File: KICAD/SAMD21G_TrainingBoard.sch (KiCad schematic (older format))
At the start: 65 parts, among them CN1 CN-PICkit4_ARM, CN2 USB_Mini_B, CN3 UART-FTDI-TTL-232R-3V3, CN4 USB_A, CN5 CN-POWER, IC1 SAMD21G18A, IC2 NJM2391DL1-33, IC3 GT20L16J1Y, SW1 SW_PUSH_2, SW2 SW_PUSH_2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

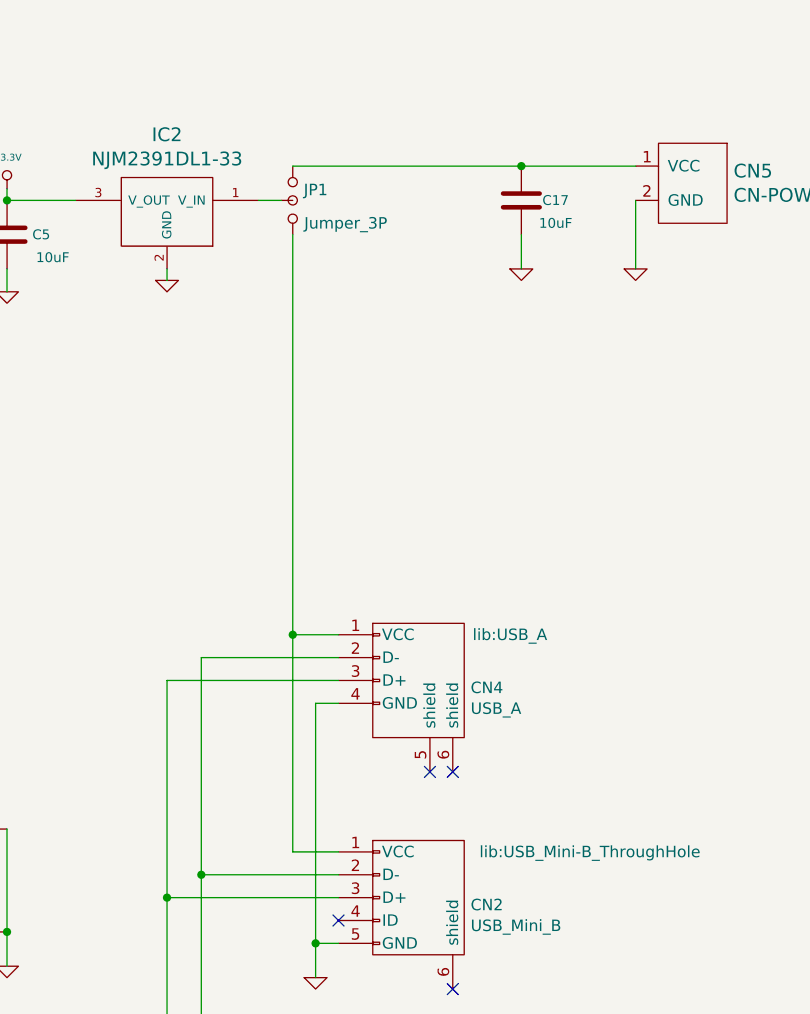
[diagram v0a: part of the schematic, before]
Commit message: amend USB Type A connector Power Supply
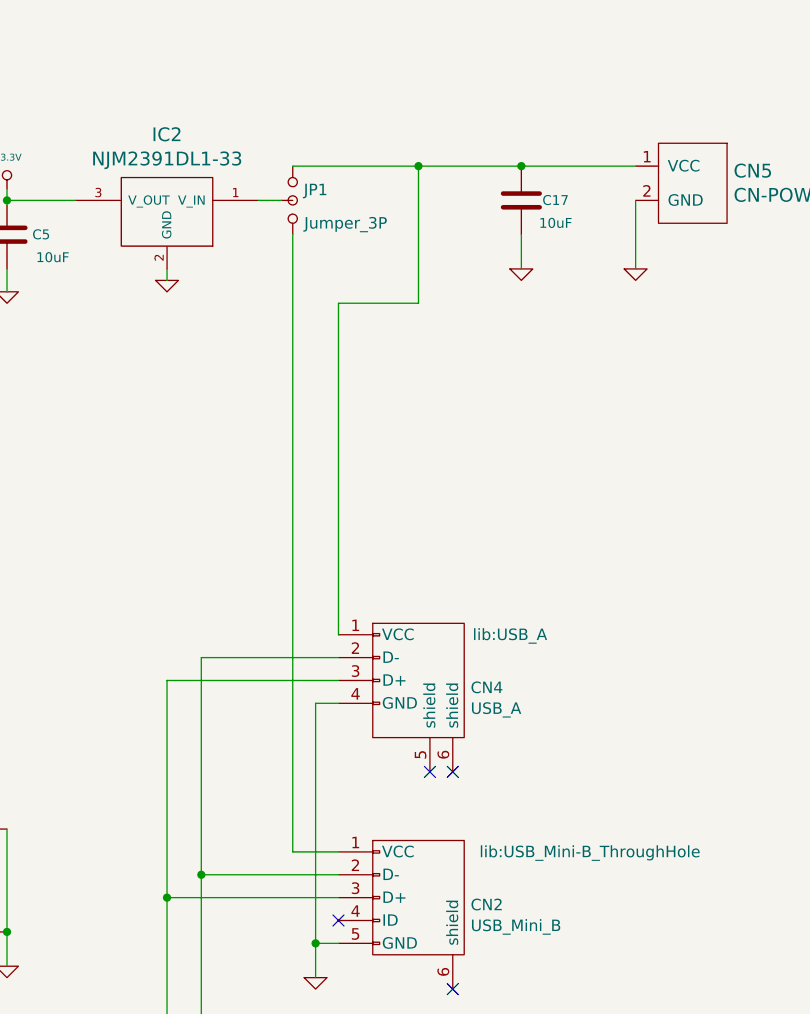
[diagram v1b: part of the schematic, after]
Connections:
- net at CN2.1 (VCC), JP1.3: no longer CN4.1 (VCC)
- net at C17.2, CN5.1 (VCC), JP1.1: now also CN4.1 (VCC)
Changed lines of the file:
@@
 	13450 4450 12850 4450
-Wire Wire Line
-	13450 3400 13250 3400
-Wire Wire Line
-	13250 3400 13250 4350
 Wire Wire Line
 	13250 4350 13450 4350
@@
 	0    1    1    0
 $EndComp
-Wire Wire Line
-	13250 3400 13250 1650
-Connection ~ 13250 3400
 $Comp
 L mylib20161223:CN-POWER CN5
@@
 $EndComp
 Wire Wire Line
-	13250 1350 14250 1350
+	13250 1350 13800 1350
 Wire Wire Line
 	13200 1500 13100 1500
@@
 Text Label 6050 5450 0    50   ~ 0
 LED4
+Wire Wire Line
+	13250 1650 13250 4350
+Wire Wire Line
+	13450 3400 13450 1950
+Wire Wire Line
+	13450 1950 13800 1950
+Wire Wire Line
+	13800 1950 13800 1350
+Connection ~ 13800 1350
+Wire Wire Line
+	13800 1350 14250 1350
 $EndSCHEMATC
